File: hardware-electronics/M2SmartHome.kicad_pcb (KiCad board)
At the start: 4 copper layers, 22 x 76 mm, 207 parts, among them J1 M.2-Key-M-edge-connector, J2 Micro_SD_Card_Det_Hirose_DM3AT, J3 CONMHF1-SMD-T, J4 CONMHF1-SMD-T, U1 RTL8188FTV-VC-CG, U10 24AA04T-I_OT, U2 EMMC16G-MW28-01E10, U3 PI7C9X440SLBFDE, U4 24AA04T-I_OT, U5 CP2102N-A02-GQFN20, U6 24AA04T-I_OT, U7 EFR32MG21B020F1024IM32-B, U8 USB2244-AEZG-06, U9 USB2244-AEZG-06, Y1 ABM8-12.000MHZ-B2-T, Y2 ECS-240-10-47-CKM-TR, Y3 ECS-240-10-47-CKM-TR, Y5 ABM8-40.000MHZ-B2-T

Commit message: [#13] WIP Placement eMMC
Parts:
- C6, R10, R11, R12, R14, R15, R16, R4: moved to B.Cu
- moved R10 33.5 mm to (83.0, 133.8), turned to 90 degrees
- moved R4 29.6 mm to (84.9, 133.9), turned to -90 degrees
- moved R7 27.4 mm to (89.2, 136.1), turned to 180 degrees
- moved R14 26.5 mm to (81.1, 131.9), turned to 180 degrees
- moved R15 25.1 mm to (81.7, 129.9), turned to 90 degrees
- moved C6 23.8 mm to (87.3, 129.8), turned to -90 degrees
- moved R16 17.2 mm to (89.4, 128.9)
- moved R13 15.5 mm to (81.7, 133.4), turned to -90 degrees
- moved R12 13.5 mm to (91.3, 132.4)
- moved R11 13.0 mm to (91.5, 131.1)
- moved C8 3.20 mm to (87.2, 131.4), turned to 0 degrees
- moved C3 1.58 mm to (89.3, 137.3)
- moved D1 0.72 mm to (91.0, 138.9)
- moved R9 0.72 mm to (93.5, 138.9)
- moved C21 0.72 mm to (92.0, 129.2)
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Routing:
- net Net-(U2-DAT2): track 0.00 -> 19.4 mm, vias 0 -> 1
- net Net-(U2-DAT4): track 0.00 -> 15.5 mm, vias 0 -> 1
- net Net-(U2-DAT3): track 0.00 -> 13.2 mm, vias 0 -> 1
- net Net-(U2-DAT1): track 0.00 -> 10.9 mm
- net Net-(U2-DAT0): track 0.77 -> 7.64 mm

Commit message: [#13] WIP Placement eMMC
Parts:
- R17, R18, R19, R20: moved to B.Cu
- moved R20 22.0 mm to (87.3, 127.3), turned to 90 degrees
- moved R19 17.1 mm to (91.1, 128.5)
- moved R18 15.8 mm to (91.1, 130.7)
- moved R17 15.6 mm to (91.1, 129.6)
- moved C22 0.90 mm to (93.4, 130.1)
- moved R11 0.81 mm to (91.1, 131.8)
- moved R12 0.54 mm to (91.1, 132.9)
- moved C21 0.45 mm to (92.2, 128.8), turned to 0 degrees
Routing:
- net Net-(U2-DAT5): track 0.00 -> 3.42 mm
- net Net-(U2-DAT6): track 0.00 -> 1.16 mm

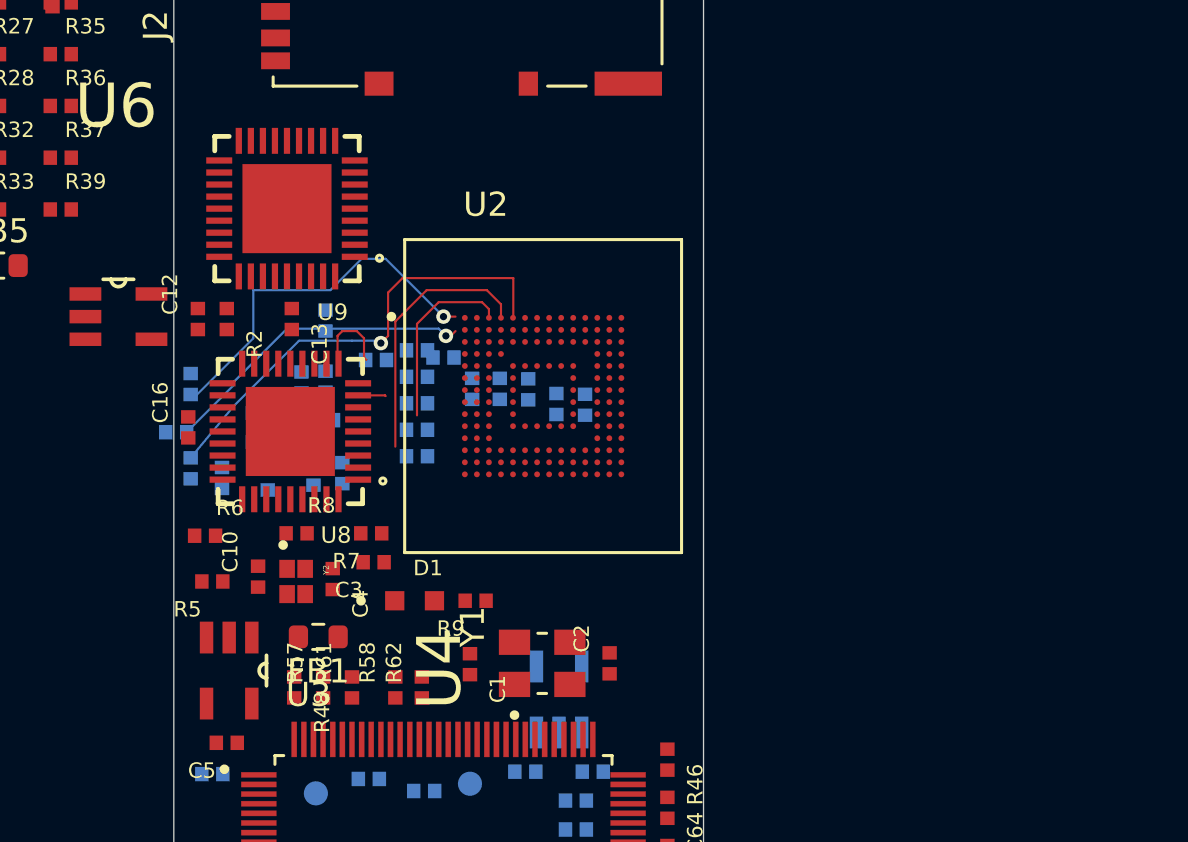
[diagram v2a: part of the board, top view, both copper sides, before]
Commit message: [#13] WIP Placement eMMC - reposition for better routing
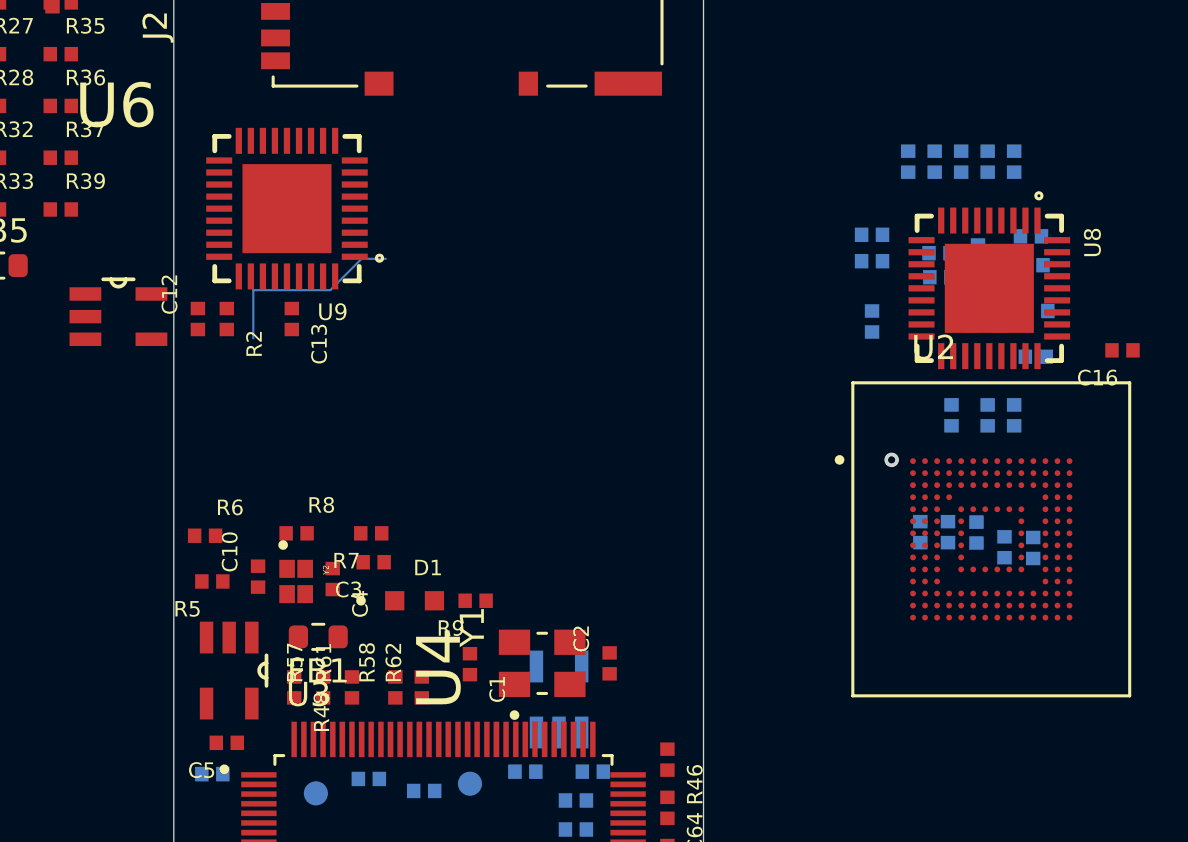
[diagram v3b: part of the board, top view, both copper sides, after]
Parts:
- moved C16 38.9 mm to (120.4, 128.5), turned to 180 degrees
- moved R13 34.3 mm to (115.9, 131.2)
- moved R10 34.2 mm to (116.8, 128.8), turned to 180 degrees
- moved R14 33.7 mm to (114.8, 131.2), turned to -90 degrees
- moved R4 32.7 mm to (116.9, 126.9), turned to 0 degrees
- moved R15 31.6 mm to (113.3, 131.2), turned to -90 degrees
- moved C9 31.1 mm to (116.7, 125.0), turned to 0 degrees
- moved C11 31.0 mm to (115.3, 127.1), turned to -90 degrees
- moved C14 30.2 mm to (116.6, 123.8), turned to 0 degrees
- moved C17 29.7 mm to (114.1, 127.1), turned to -90 degrees
- moved U8 29.6 mm to (114.9, 125.9), turned to -90 degrees
- moved C8 28.0 mm to (114.4, 124.6), turned to 90 degrees
- moved R12 27.7 mm to (115.9, 120.7), turned to 90 degrees
- moved C7 26.9 mm to (112.8, 125.5), turned to 180 degrees
- moved R11 26.2 mm to (114.8, 120.7), turned to 90 degrees
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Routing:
- net Net-(U2-DAT2): track 19.4 -> 0.00 mm, vias 1 -> 0
- net Net-(U2-DAT3): track 13.2 -> 0.00 mm, vias 1 -> 0
- net Net-(U2-DAT1): track 10.9 -> 0.00 mm
- net Net-(U2-DAT0): track 7.64 -> 0.00 mm
- net Net-(U2-DAT4): track 15.5 -> 8.04 mm
- net Net-(U2-DAT5): track 3.42 -> 0.00 mm
- net Net-(U2-DAT6): track 1.16 -> 0.00 mm

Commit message: [#13] WIP Placement eMMC
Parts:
- C12, R2, R34: moved to B.Cu
- moved FB5 31.2 mm to (101.2, 139.7)
- moved R34 29.3 mm to (98.8, 132.9), turned to 90 degrees
- moved Y3 27.8 mm to (97.4, 130.1), turned to 180 degrees
- moved C15 27.2 mm to (86.0, 134.1)
- moved C16 27.2 mm to (93.3, 126.5)
- moved C8 27.2 mm to (87.3, 122.6)
- moved C9 27.2 mm to (89.5, 123.0)
- moved R12 27.2 mm to (88.8, 118.7)
- moved R13 27.2 mm to (88.8, 129.2)
- moved R18 27.2 mm to (86.6, 118.7)
- moved U2 27.2 mm to (87.8, 134.4)
- moved U8 27.2 mm to (87.7, 124.0)
- moved R11 27.2 mm to (87.7, 118.7)
- moved R17 27.2 mm to (85.5, 118.7)
- moved R19 27.2 mm to (84.4, 118.7)
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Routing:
- net Net-(U2-DAT4): track 8.04 -> 0.00 mm, vias 1 -> 0

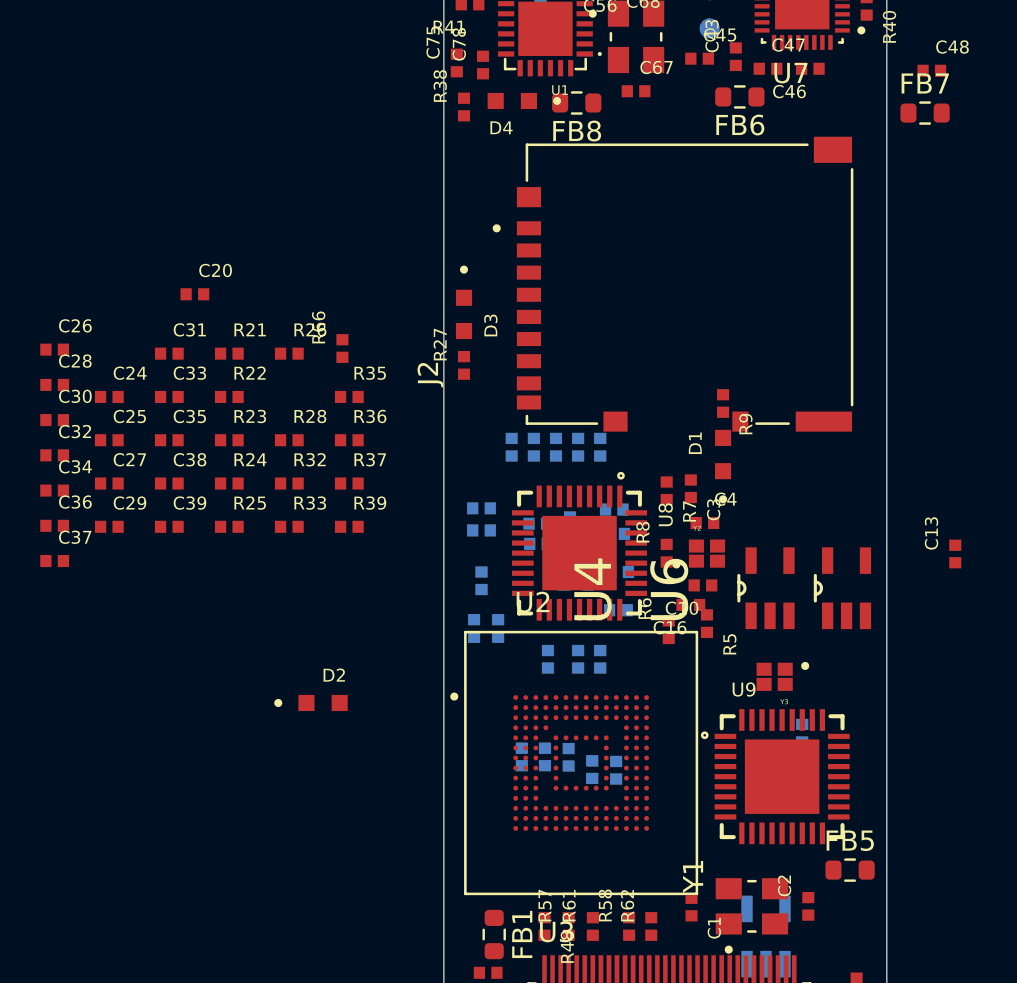
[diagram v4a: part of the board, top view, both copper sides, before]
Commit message: [#13] WIP Placement uSD
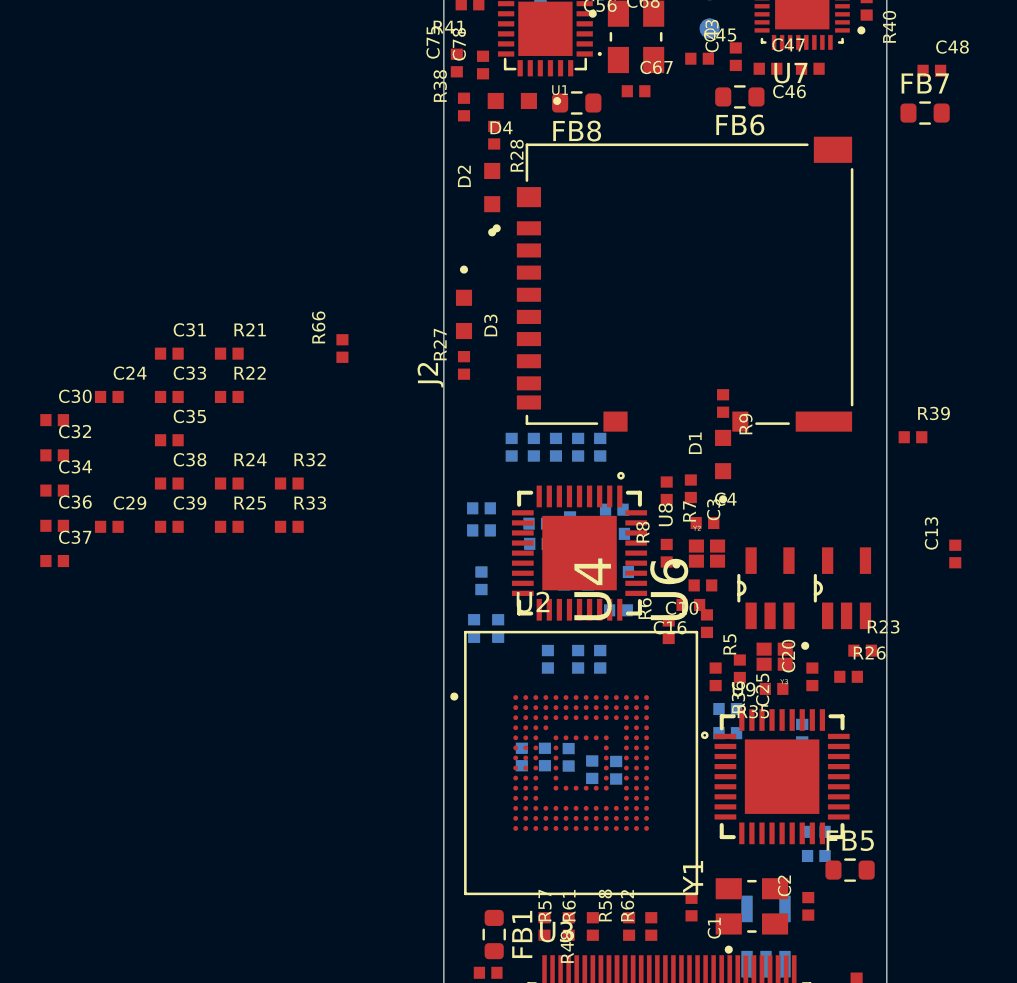
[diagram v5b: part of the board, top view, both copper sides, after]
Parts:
- C26, C27, C28, R37: moved to B.Cu
- moved C26 45.4 mm to (99.5, 139.0)
- moved C28 37.1 mm to (95.1, 131.7)
- moved C20 36.1 mm to (99.3, 130.1), turned to 90 degrees
- moved C25 33.3 mm to (95.7, 129.7), turned to -90 degrees
- moved R23 33.1 mm to (101.8, 128.8)
- moved C27 33.1 mm to (95.1, 132.9)
- moved R26 32.1 mm to (101.1, 130.1)
- moved R37 28.9 mm to (99.5, 137.8), turned to 180 degrees
- moved R39 28.3 mm to (104.3, 118.2)
- moved D2 26.9 mm to (83.4, 105.8), turned to 90 degrees
- moved R35 25.6 mm to (97.4, 130.7), turned to 180 degrees
- moved R36 21.7 mm to (94.5, 130.1), turned to -90 degrees
- moved R28 18.2 mm to (83.5, 103.2), turned to -90 degrees
- moved Y3 1.00 mm to (97.4, 129.1)

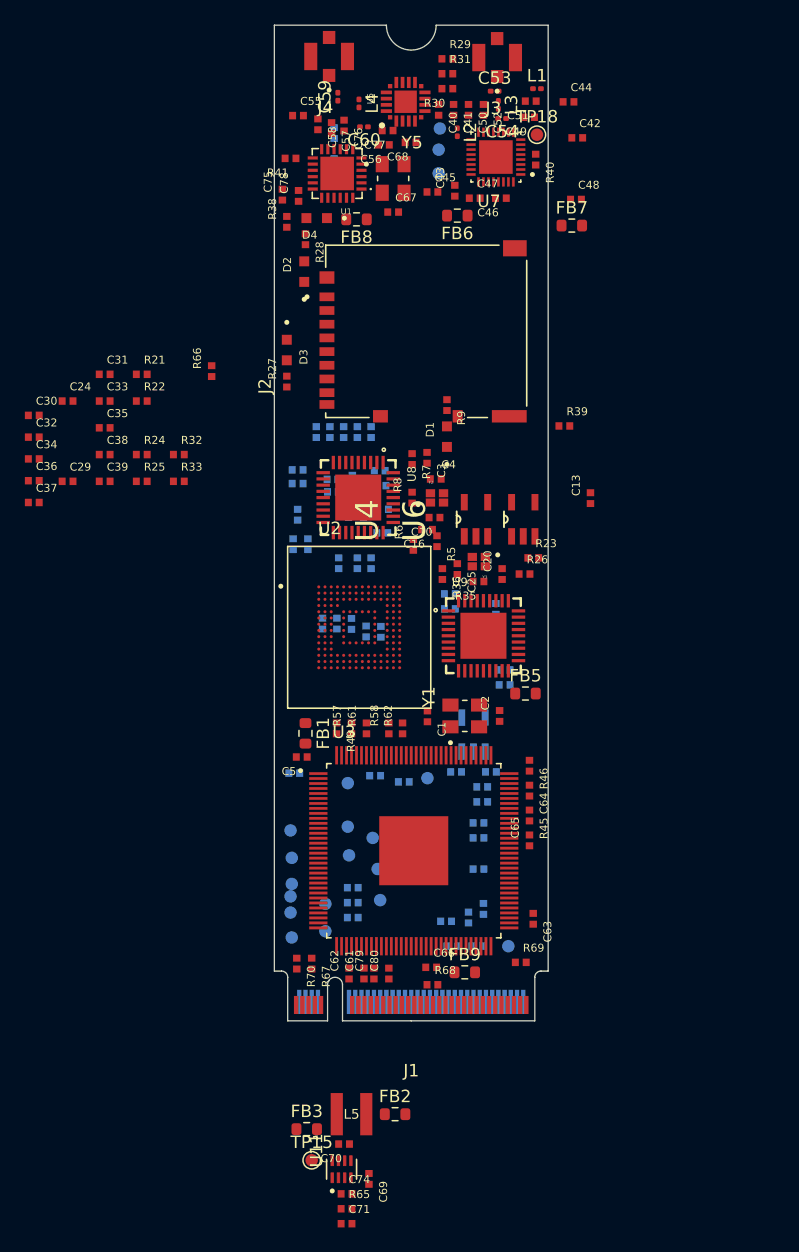
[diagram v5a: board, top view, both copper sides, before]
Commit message: [#13] WIP Placement uSD
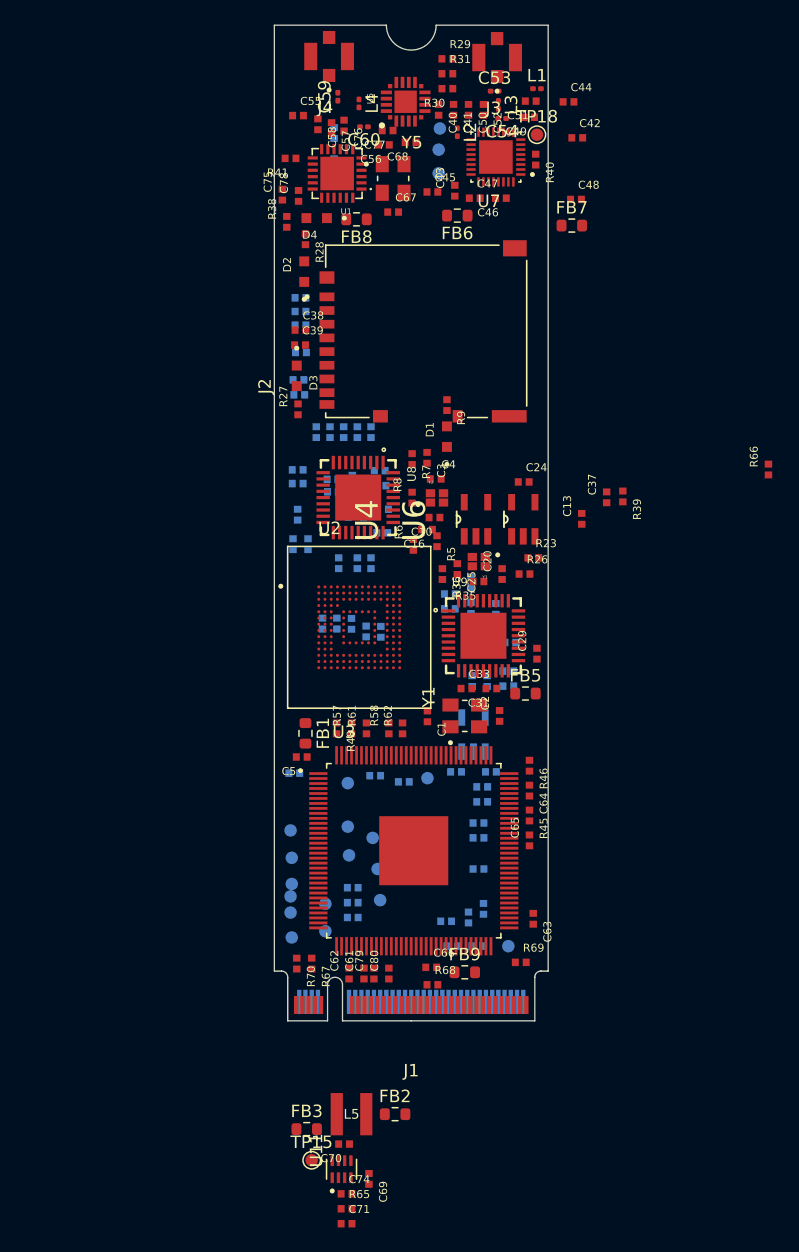
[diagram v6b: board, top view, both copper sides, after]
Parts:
- C30, C32, C34, C35, C36, R21, R22, R24, R25, R32, R33: moved to B.Cu
- moved C37 46.0 mm to (107.7, 123.9), turned to 90 degrees
- moved R66 45.4 mm to (120.7, 121.7)
- moved C30 42.4 mm to (100.0, 135.6)
- moved C32 41.4 mm to (98.1, 138.7), turned to -90 degrees
- moved C29 40.2 mm to (102.1, 136.5), turned to 90 degrees
- moved C31 40.0 mm to (98.4, 139.3), turned to 180 degrees
- moved C34 39.5 mm to (96.9, 138.7), turned to -90 degrees
- moved C24 37.2 mm to (101.0, 122.7)
- moved C33 37.1 mm to (96.4, 139.3)
- moved C36 36.1 mm to (96.8, 130.8), turned to -90 degrees
- moved C35 32.8 mm to (96.8, 132.8), turned to 90 degrees
- moved C39 19.1 mm to (83.1, 111.7)
- moved R25 18.7 mm to (83.1, 109.0), turned to 180 degrees
- moved C38 18.6 mm to (83.1, 110.5)
- moved R24 17.9 mm to (83.1, 107.9), turned to 180 degrees
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
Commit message: [#15] Defined track widths
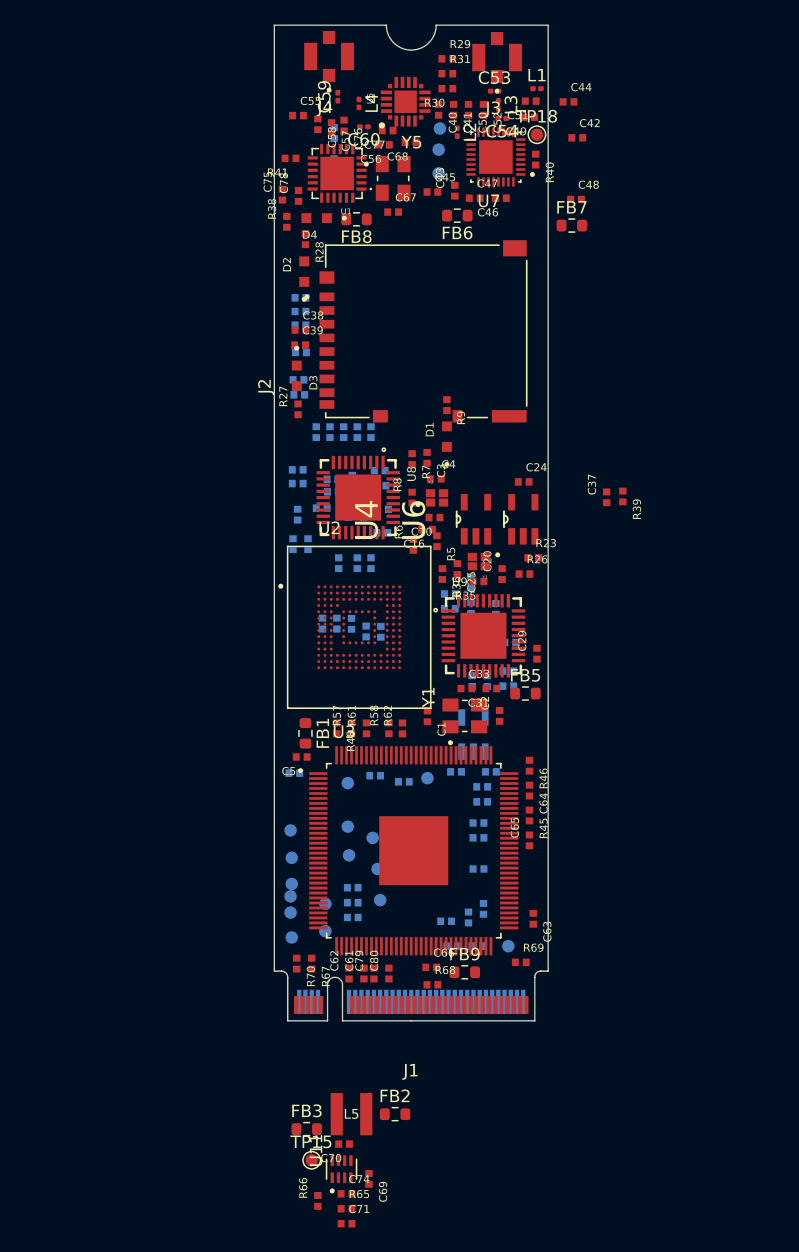
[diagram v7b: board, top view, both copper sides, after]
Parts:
- C13: moved to B.Cu
- moved R66 69.0 mm to (84.5, 180.5)
- moved C13 20.9 mm to (84.8, 124.8), turned to 180 degrees
